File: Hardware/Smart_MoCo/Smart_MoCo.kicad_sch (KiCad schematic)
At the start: 30 parts, among them J1 Conn_01x04, J2 1722861102, J3 Conn_01x02, J4 1722861102, J5 Conn_01x04, J6 Conn_01x02, J7 Conn_01x02, U1 STM32F042F6Px, U2 VNH5019A-E, U3 SN65HVD232, U4 AP62200WU

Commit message: Update gerbs and bom
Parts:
- renumbered C2 to C1, C7 to C2, C10 to C3, J3 to J1, J5 to J2, J6 to J3, J7 to J4, J1 to J5, J4 to J6, J2 to J7, L2 to L1, R4 to R1, R12 to R10, R8 to R4, R9 to R5, R5 to R6, R6 to R7, R10 to R8, R11 to R9
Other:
- moved on the sheet: J5

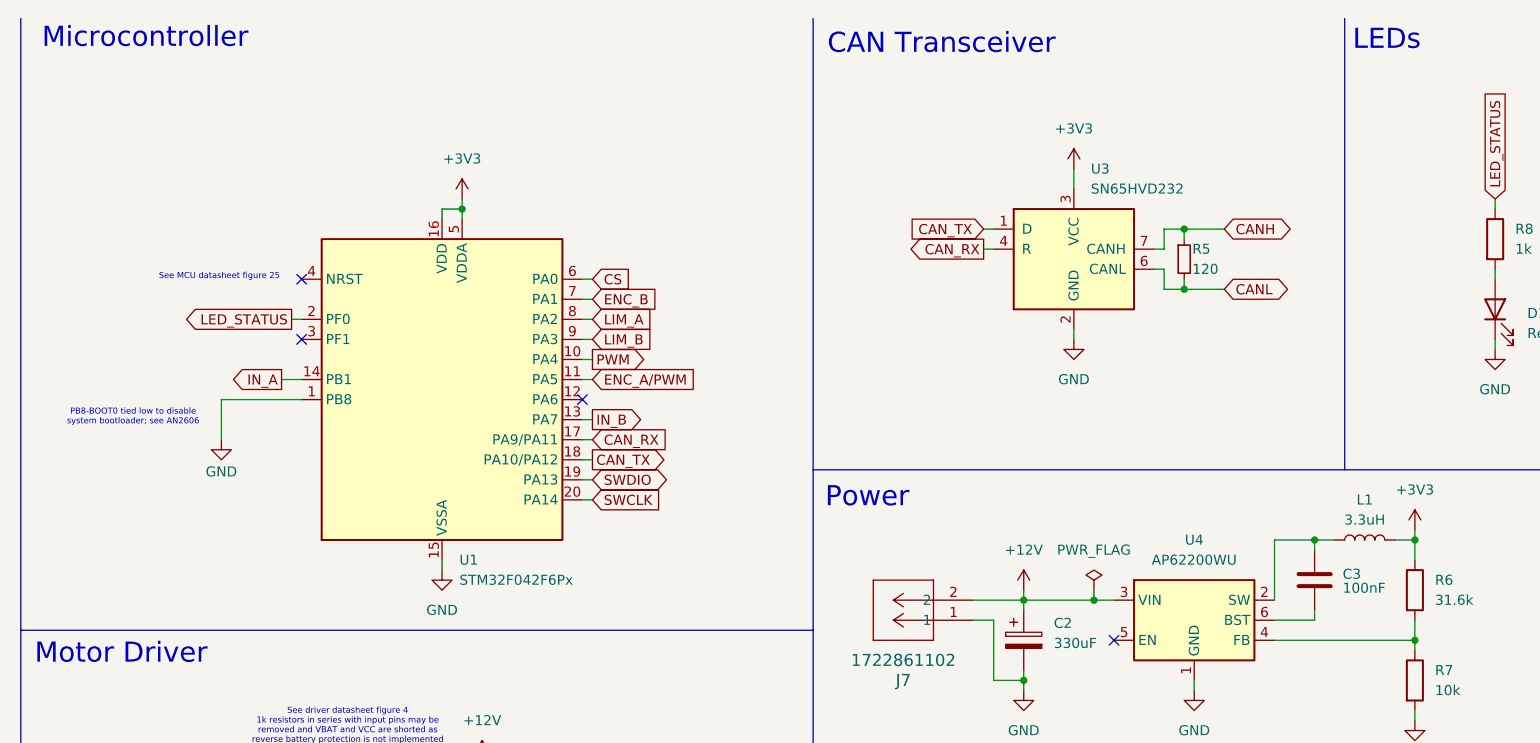
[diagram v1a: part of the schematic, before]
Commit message: Added bulk capacitors and kicad github action
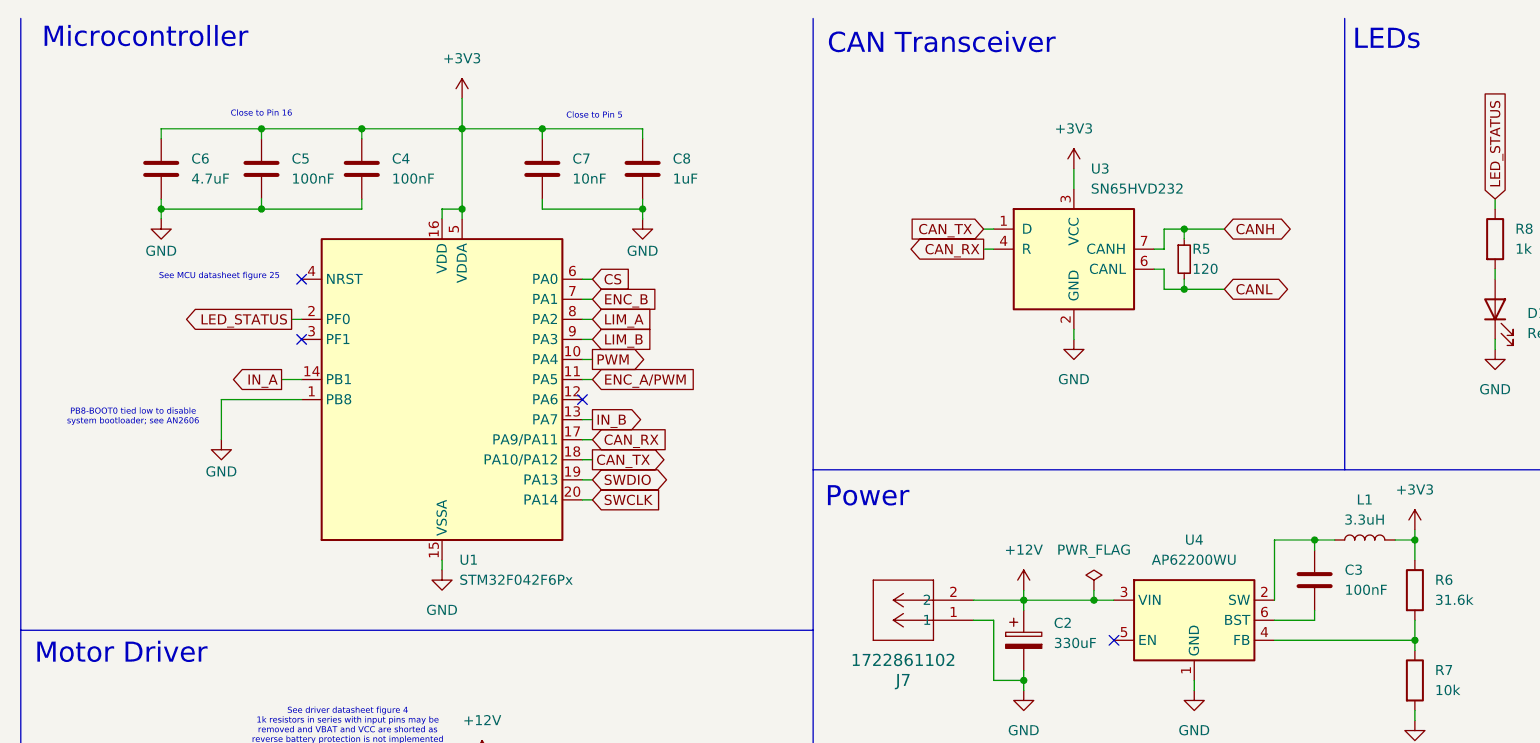
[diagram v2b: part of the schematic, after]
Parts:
- added C4, C5: 100nF, Capacitor_SMD:C_0402_1005Metric_Pad0.74x0.62mm_HandSolder, symbol Device:C
- added C6: 4.7uF, Capacitor_SMD:C_0402_1005Metric_Pad0.74x0.62mm_HandSolder, symbol Device:C
- added C7: 10nF, Capacitor_SMD:C_0402_1005Metric_Pad0.74x0.62mm_HandSolder, symbol Device:C
- added C8: 1uF, Capacitor_SMD:C_0402_1005Metric_Pad0.74x0.62mm_HandSolder, symbol Device:C
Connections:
- net +3V3: now also C4.1, C5.1, C6.1, C7.1, C8.1
- net GND: now also C4.2, C5.2, C6.2, C7.2, C8.2
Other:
- note added: "Close to Pin 16"
- note added: "Close to Pin 5"
